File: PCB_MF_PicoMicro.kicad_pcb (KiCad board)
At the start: 2 copper layers, 36.5 x 18.5 mm, 41 parts, among them J3 USB_C_Receptacle_USB2.0_16P, J7 Conn_01x02_Pin, J8 Conn_01x02_Pin, SW1 SW_Push, U1 RP2040, U2 AMS1117-3.3, U4 W25Q16JVSS, U5 ProMicro, Y1 X322512MSB4SI

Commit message: minor layout optimazations, update production files
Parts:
- moved D3 0.93 mm to (111.9, 87.2)
- moved R9 0.93 mm to (111.9, 86.2)
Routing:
- net Net-(J3-CC1): track 5.17 -> 13.5 mm
- net D13: track 16.8 -> 20.0 mm
- net D15: track 17.1 -> 20.2 mm
- net D14: track 17.3 -> 20.1 mm
- net VIN: track 27.0 -> 25.6 mm
- net TX1: track 13.0 -> 14.1 mm
- net D10: track 21.3 -> 22.1 mm
- net RX1: track 13.4 -> 14.1 mm
- net /RP2350A/GPIO11: track 3.50 -> 3.11 mm, vias 0 -> 2
- net 3.3V: track 83.9 -> 83.5 mm, vias 11 -> 12
- removed copper zone on F.Cu, net 3.3V

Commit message: update production files acc. order
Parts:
- R10, R9: value 150 -> 200
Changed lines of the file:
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@@
 			)
 		)
-		(property "Value" "150"
+		(property "Value" "200"
 			(at 0 1.17 0)
 			(layer "F.Fab")
@@
 			)
 		)
-		(property "Value" "150"
+		(property "Value" "200"
 			(at 0 1.17 0)
 			(layer "F.Fab")
@@
 			)
 		)
-		(property "MPN - JLCPCB" "C9002"
+		(property "MPN - JLCPCB" "C20625731"
 			(at 0 0 0)
 			(layer "F.Fab")

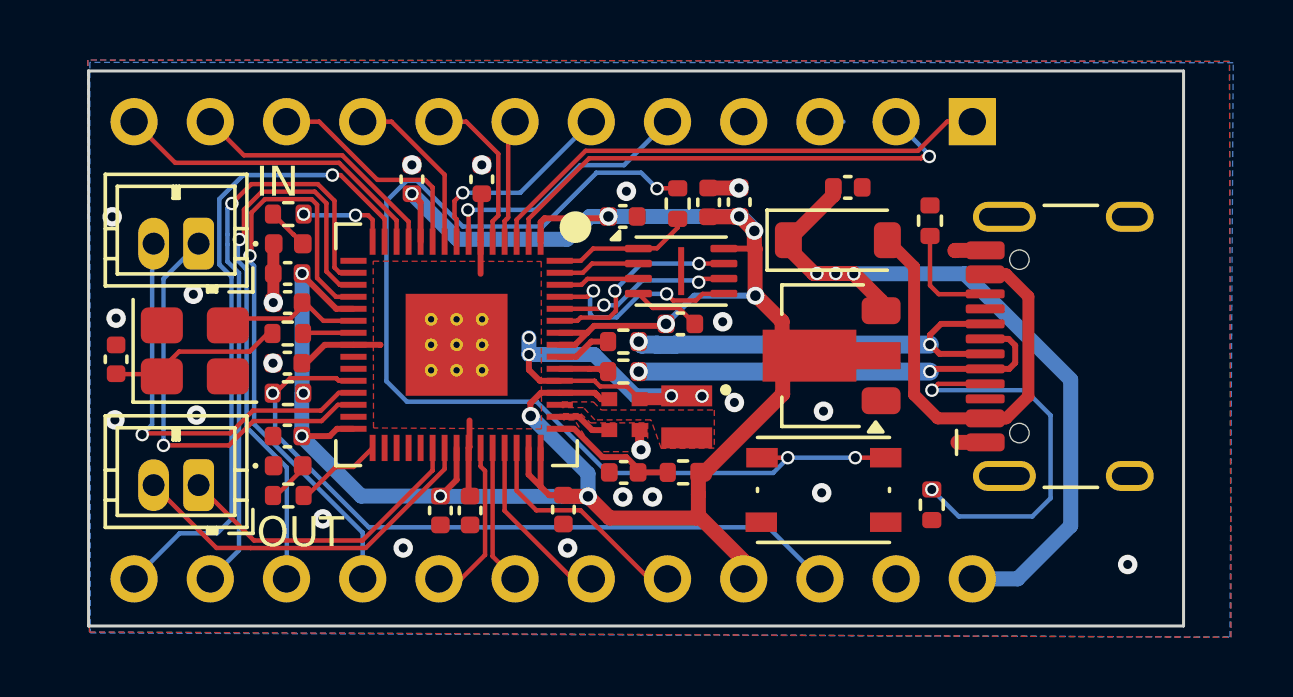
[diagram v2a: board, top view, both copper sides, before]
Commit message: replace ProMicro against pin header connectors
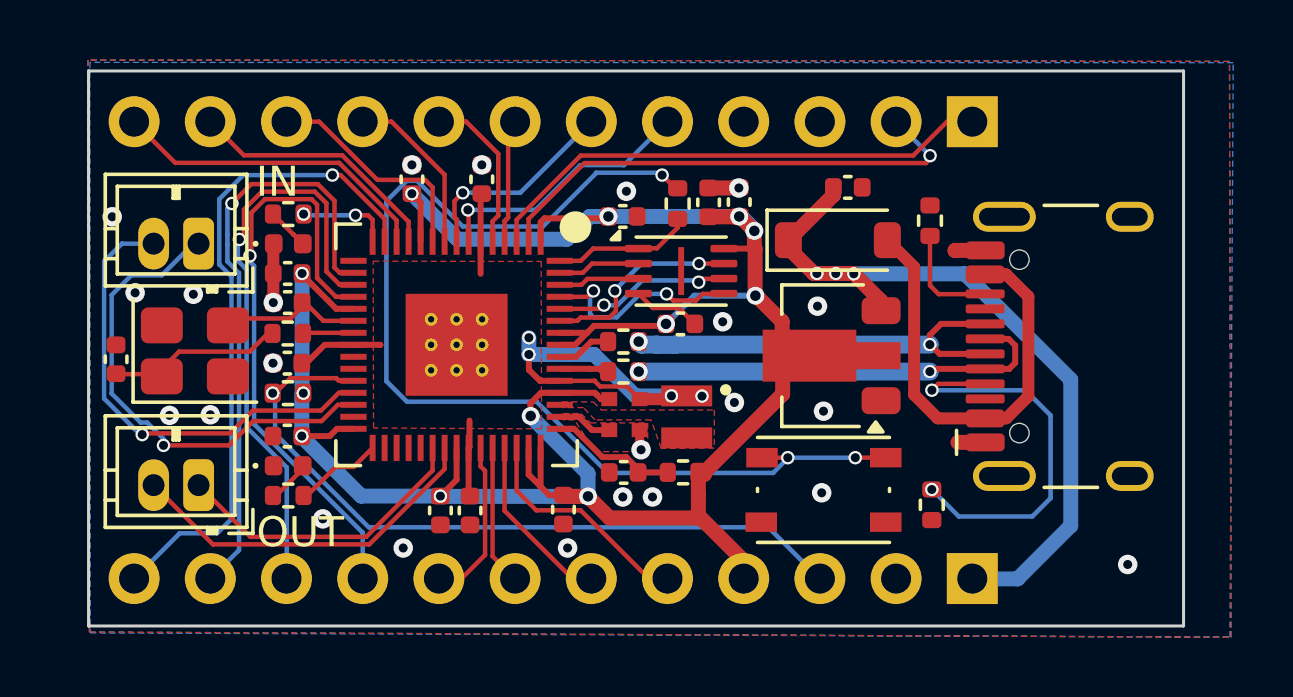
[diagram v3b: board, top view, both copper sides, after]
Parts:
- removed U5: ProMicro, _Own_Library:ProMicro
- added J1: Conn_01x12, Connector_PinHeader_2.54mm:PinHeader_1x12_P2.54mm_Vertical, B.Cu at (134.7, 83.1)
- added J2: Conn_01x12, Connector_PinHeader_2.54mm:PinHeader_1x12_P2.54mm_Vertical, B.Cu at (134.7, 98.3)
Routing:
- net RX1: track 14.1 -> 16.4 mm
- net TX1: track 14.1 -> 15.9 mm
- net GND: vias 22 -> 23
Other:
- board text added: "PicoMicroMS V1.1 ??/25"
- board text removed: "PicoMicroMS V1.0 08/25"

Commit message: change ProMicro footprint to standard connector
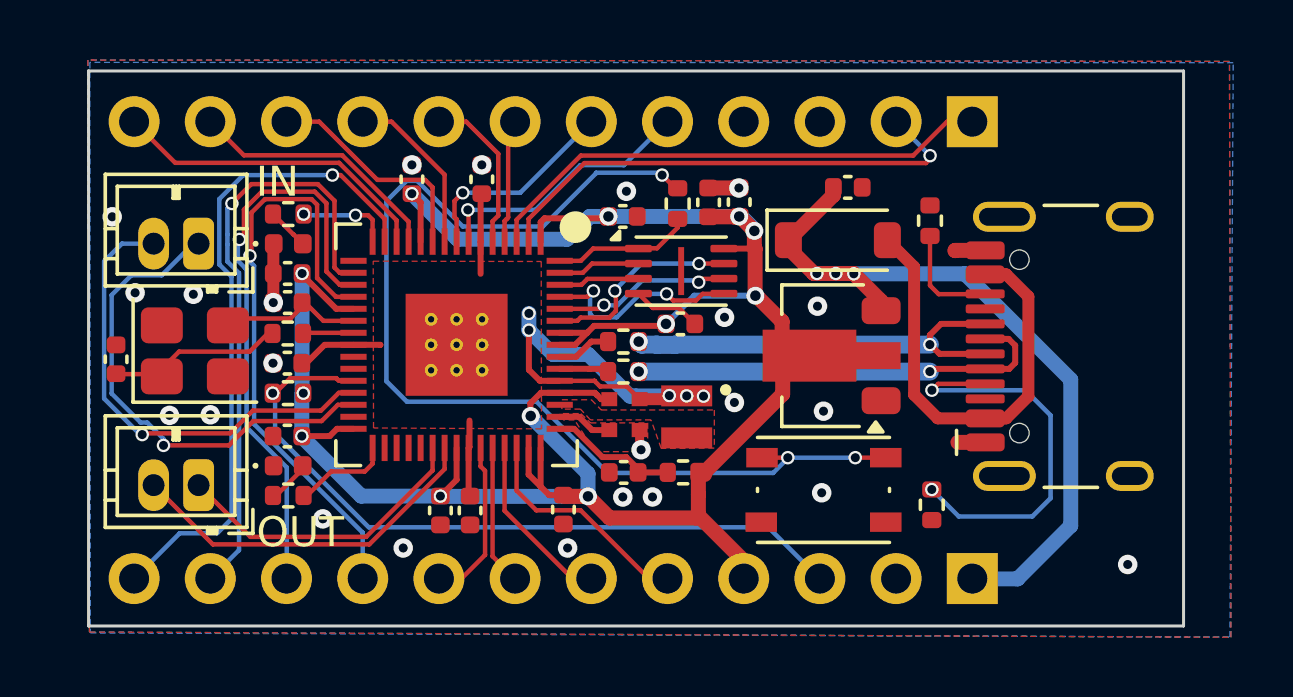
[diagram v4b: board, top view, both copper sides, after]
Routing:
- net +1V1: track 21.9 -> 23.0 mm, vias 4 -> 5
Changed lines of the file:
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@@
 		(tags "Through hole pin header THT 1x12 2.54mm single row")
 		(property "Reference" "J2"
-			(at 0 2.38 -90)
+			(at 0 2.38 270)
 			(layer "B.SilkS")
 			(hide yes)
@@
 		)
 		(property "Value" "Conn_01x12"
-			(at 0 -30.32 -90)
+			(at 0 -30.32 270)
 			(layer "B.Fab")
 			(effects
@@
 		)
 		(property "Datasheet" "~"
-			(at 0 0 -90)
+			(at 0 0 270)
 			(layer "B.Fab")
 			(hide yes)
@@
 		)
 		(property "Description" "Generic connector, single row, 01x12, script generated (kicad-library-utils/schlib/autogen/connector/)"
-			(at 0 0 -90)
+			(at 0 0 270)
 			(layer "B.Fab")
 			(hide yes)
@@
 		(tags "Through hole pin header THT 1x12 2.54mm single row")
 		(property "Reference" "J1"
-			(at 0 2.38 -90)
+			(at 0 2.38 270)
 			(layer "B.SilkS")
 			(hide yes)
@@
 		)
 		(property "Value" "Conn_01x12"
-			(at 0 -30.32 -90)
+			(at 0 -30.32 270)
 			(layer "B.Fab")
 			(effects
@@
 		)
 		(property "Datasheet" "~"
-			(at 0 0 -90)
+			(at 0 0 270)
 			(layer "B.Fab")
 			(hide yes)
@@
 		)
 		(property "Description" "Generic connector, single row, 01x12, script generated (kicad-library-utils/schlib/autogen/connector/)"
-			(at 0 0 -90)
+			(at 0 0 270)
 			(layer "B.Fab")
 			(hide yes)
@@
 	)
 	(gr_text "PicoMicroMS\nV1.1\n??/25"
-		(at 123.3 92.95 0)
+		(at 136.5 92.36 0)
 		(layer "B.SilkS")
 		(effects
@@
 	)
 	(via
-		(at 126.37 89.78)
+		(at 126.43 89.63)
 		(size 0.65)
 		(drill 0.3)
@@
 	)
 	(segment
-		(start 119.91 90.87)
-		(end 119.91 91.38)
-		(width 0.2)
-		(layer "F.Cu")
-		(net 5)
-	)
-	(segment
 		(start 114.9575 90.5475)
 		(end 114.96 90.55)
@@
 	)
 	(segment
-		(start 112.49 91.16)
-		(end 113.1025 90.5475)
+		(start 119.91 91.38)
+		(end 120.2775 91.7475)
 		(width 0.2)
 		(layer "F.Cu")
@@
 	)
 	(segment
-		(start 120.2775 91.7475)
-		(end 120.9375 91.7475)
+		(start 112.49 91.16)
+		(end 113.1025 90.5475)
 		(width 0.2)
 		(layer "F.Cu")
@@
 	)
 	(segment
-		(start 119.91 91.38)
-		(end 120.2775 91.7475)
-		(width 0.2)
-		(layer "F.Cu")
-		(net 5)
-	)
-	(segment
 		(start 122.104 91.754)
 		(end 122.104 91.757562)
@@
 	)
 	(segment
+		(start 119.91 90.06)
+		(end 119.91 91.38)
+		(width 0.2)
+		(layer "F.Cu")
+		(net 5)
+	)
+	(segment
 		(start 118.3 87.11)
 		(end 118.3 88.18)
@@
 		(net 5)
 	)
+	(segment
+		(start 120.2775 91.7475)
+		(end 120.9375 91.7475)
+		(width 0.2)
+		(layer "F.Cu")
+		(net 5)
+	)
+	(via
+		(at 124.59 92.24)
+		(size 0.45)
+		(drill 0.3)
+		(layers "F.Cu" "B.Cu")
+		(net 5)
+	)
 	(via
-		(at 124.66 92.25)
+		(at 119.91 90.06)
 		(size 0.45)
 		(drill 0.3)
@@
 	)
 	(via
-		(at 119.91 90.87)
+		(at 125.73 92.26)
 		(size 0.45)
 		(drill 0.3)
@@
 	)
 	(via
-		(at 125.68 92.26)
+		(at 119.91 89.5)
 		(size 0.45)
 		(drill 0.3)
@@
 	)
 	(via
-		(at 119.91 90.31)
+		(at 125.17 92.25)
 		(size 0.45)
 		(drill 0.3)
@@
 	)
 	(segment
+		(start 121.89 90.87)
+		(end 123.279346 92.259346)
+		(width 0.5)
+		(layer "B.Cu")
+		(net 5)
+	)
+	(segment
 		(start 125.67 92.25)
 		(end 124.66 92.25)
@@
 	)
 	(segment
-		(start 122.08 90.87)
-		(end 123.469346 92.259346)
+		(start 123.469346 92.25)
+		(end 124.65 92.25)
 		(width 0.5)
 		(layer "B.Cu")
@@
 	)
 	(segment
-		(start 123.469346 92.25)
-		(end 124.65 92.25)
+		(start 120.72 90.87)
+		(end 121.89 90.87)
+		(width 0.5)
+		(layer "B.Cu")
+		(net 5)
+	)
+	(segment
+		(start 119.91 90.06)
+		(end 120.72 90.87)
 		(width 0.5)
 		(layer "B.Cu")
@@
 	)
 	(segment
-		(start 119.91 90.87)
-		(end 122.08 90.87)
+		(start 119.91 89.5)
+		(end 119.91 90.06)
 		(width 0.5)
 		(layer "B.Cu")
@@
 	)
 	(segment
-		(start 119.91 90.31)
-		(end 119.91 90.87)
+		(start 123.279346 92.259346)
+		(end 123.469346 92.259346)
 		(width 0.5)
 		(layer "B.Cu")
@@
 	)
 	(segment
-		(start 114.065 94.62)
-		(end 114.7 93.985)
+		(start 114.44 94.77)
+		(end 114.7 94.51)
 		(width 0.15)
 		(layer "F.Cu")
@@
 	)
 	(segment
-		(start 112.47 95.62)
-		(end 113.47 94.62)
+		(start 113.32 94.77)
+		(end 114.44 94.77)
+		(width 0.15)
+		(layer "F.Cu")
+		(net 32)
+	)
+	(segment
+		(start 114.7 94.51)
+		(end 114.7 93.985)
 		(width 0.15)
 		(layer "F.Cu")
@@
 	)
 	(segment
-		(start 113.47 94.62)
-		(end 114.065 94.62)
+		(start 112.47 95.62)
+		(end 113.32 94.77)
 		(width 0.15)
 		(layer "F.Cu")
@@
 		(polygon
 			(pts
-				(xy 121.01 92.45) (xy 122.061481 92.45) (xy 122.321481 92.72) (xy 126.09 92.72) (xy 126.09 93.99)
-				(xy 124.32 94) (xy 123.98 93.05) (xy 122.11 93.05) (xy 121.73 92.64) (xy 121.01 92.64)
+				(xy 121.01 92.38) (xy 121.994074 92.38) (xy 122.321481 92.72) (xy 126.09 92.72) (xy 126.09 93.99)
+				(xy 124.32 94) (xy 123.98 93.05) (xy 121.961457 93.05) (xy 121.627799 92.69) (xy 121.01 92.69)
 			)
 		)

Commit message: add cap for AVDD, fix wrong cap value 1V1
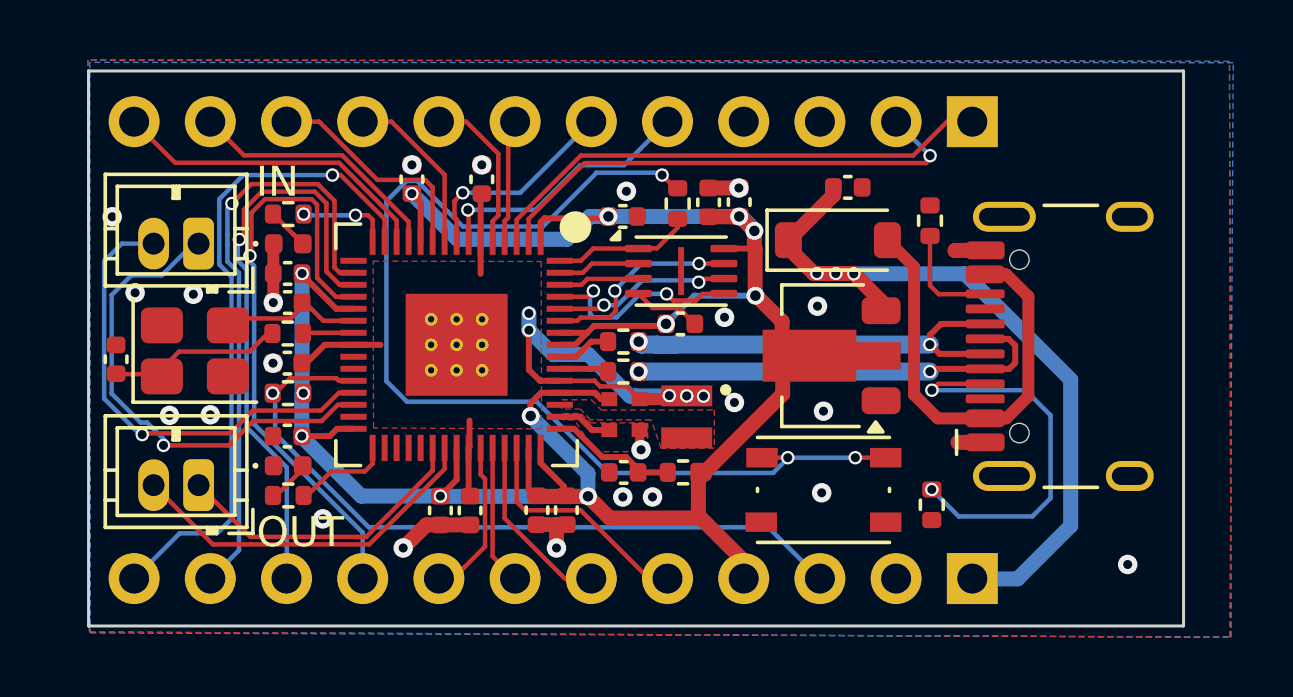
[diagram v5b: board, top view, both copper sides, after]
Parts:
- added C19: 4.7uF, Capacitor_SMD:C_0402_1005Metric, F.Cu at (120.2, 96.1)
- C7: value 4.7uF -> 100nF
- moved C10 0.10 mm to (121.2, 96.1)
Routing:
- net GND: track 11.3 -> 15.6 mm
- net 3.3V: track 83.5 -> 84.5 mm

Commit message: better routing of USB_BOOT track
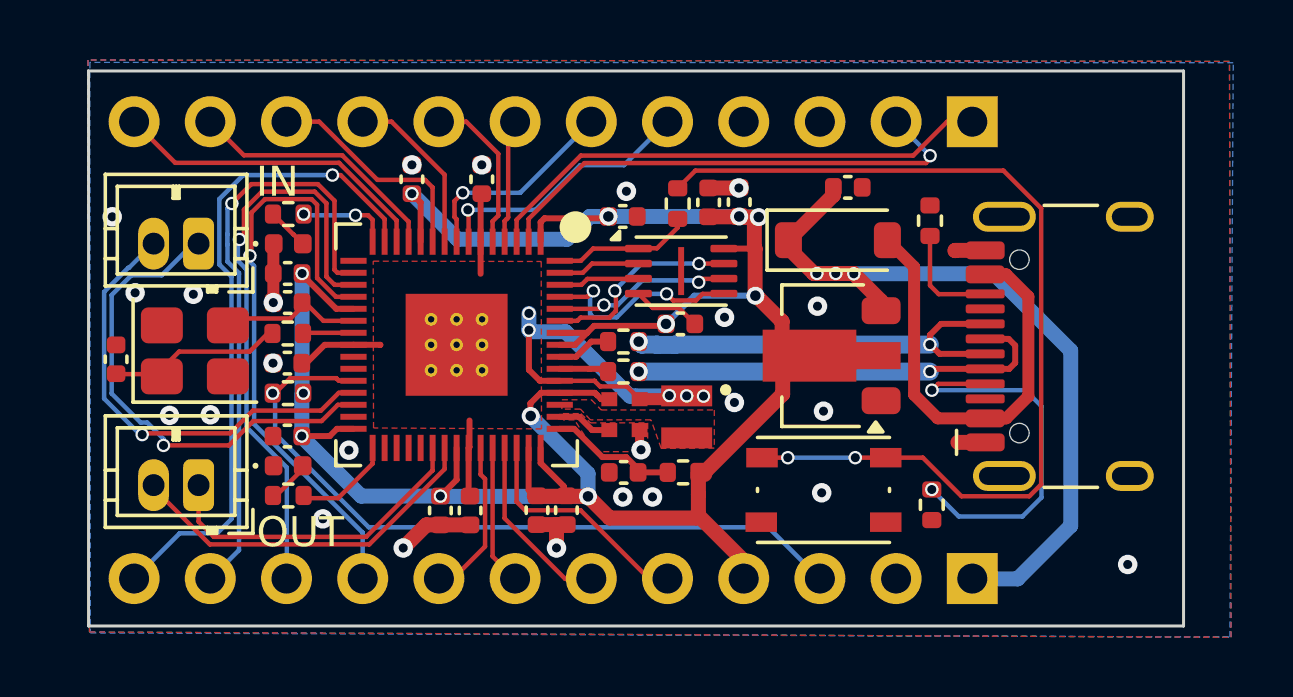
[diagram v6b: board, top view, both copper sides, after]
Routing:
- net /RP2350A/~{USB_BOOT}: track 36.6 -> 32.2 mm, vias 3 -> 2
- net TX2: track 10.4 -> 11.1 mm
- net TX1: track 15.9 -> 15.3 mm
- net VIN: track 25.6 -> 26.2 mm
- net GND: vias 23 -> 24

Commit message: serial resistor for TX line
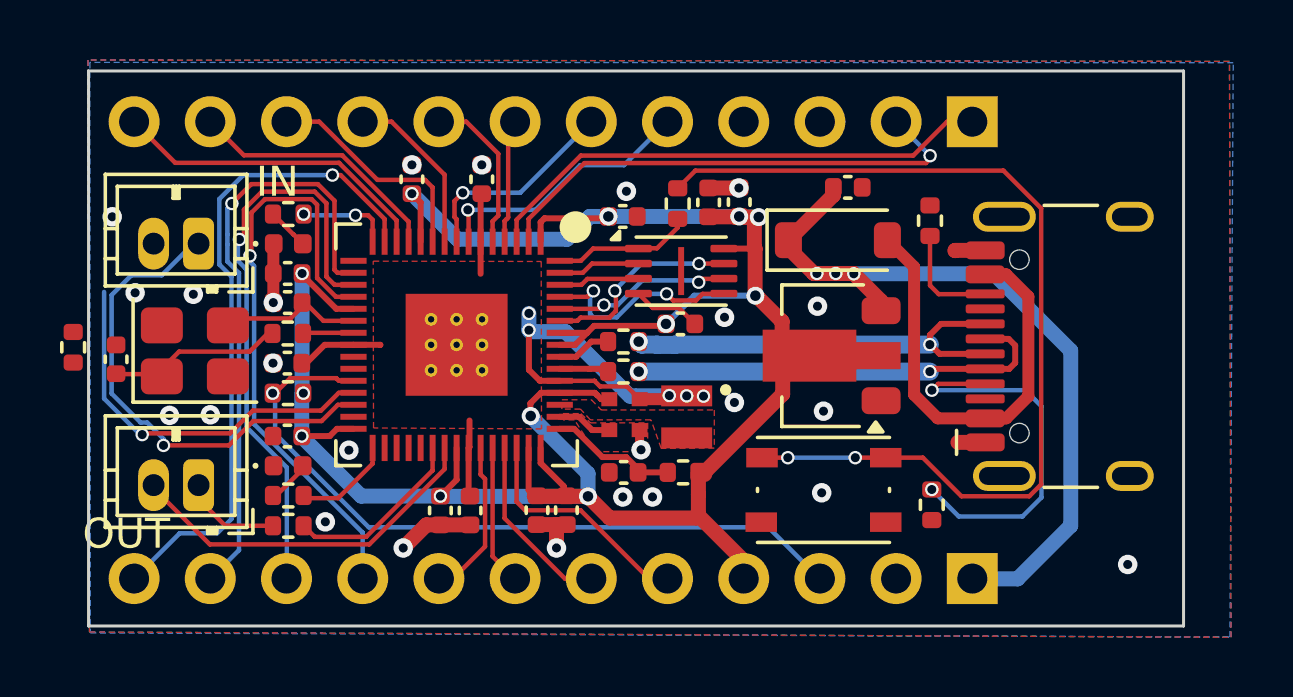
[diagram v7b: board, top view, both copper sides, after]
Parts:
- added R11: 100, Resistor_SMD:R_0402_1005Metric, F.Cu at (104.7, 90.6)
- added R12: 100, Resistor_SMD:R_0402_1005Metric, F.Cu at (111.9, 96.6)
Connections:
- J7 pad 2: TX1 -> Net-(J7-Pin_2)
- J8 pad 1: TX2 -> Net-(J8-Pin_1)
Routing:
- net TX2: track 11.1 -> 6.12 mm
- net Net-(J8-Pin_1): track 0.00 -> 3.52 mm
- net TX1: track 15.3 -> 12.9 mm

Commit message: route both additional resistors
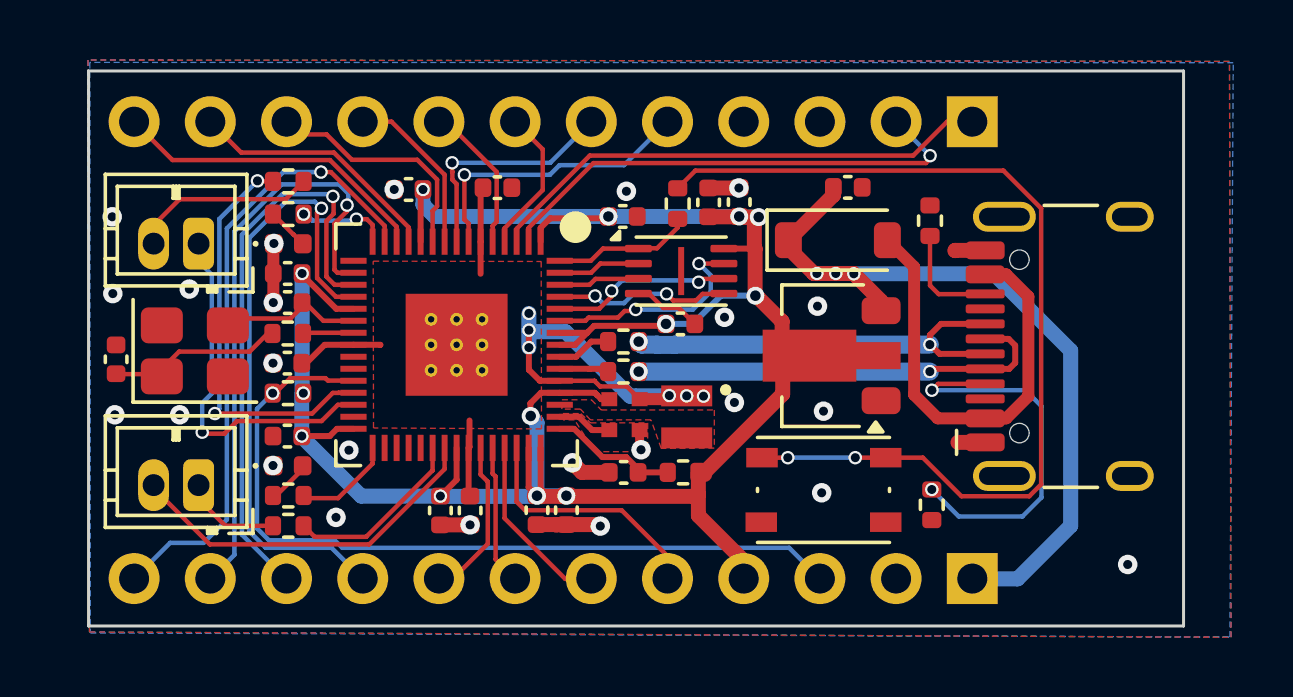
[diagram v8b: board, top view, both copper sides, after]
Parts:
- moved R11 9.05 mm to (111.9, 85.1), turned to 180 degrees
- moved C6 0.59 mm to (118.9, 85.3), turned to 0 degrees
- moved C13 0.36 mm to (115.9, 85.4), turned to 180 degrees
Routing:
- net Net-(J7-Pin_2): track 0.02 -> 6.23 mm
- net RX1: track 16.4 -> 12.2 mm
- net RST: track 25.0 -> 27.6 mm
- net 3.3V: track 84.9 -> 82.5 mm, vias 12 -> 13
- net /RP2350A/QSPI_SD0: track 6.74 -> 5.54 mm
- net D10: track 22.1 -> 20.9 mm
- net D15: track 20.2 -> 21.1 mm
- net D5: track 7.33 -> 8.19 mm
- net TX1: track 12.9 -> 13.8 mm, vias 1 -> 2
- net D4: track 9.51 -> 10.4 mm
- net D2: track 4.15 -> 4.91 mm
- net /RP2350A/QSPI_SD3: track 6.36 -> 7.01 mm
- net +1V1: track 23.0 -> 23.6 mm, vias 5 -> 6
